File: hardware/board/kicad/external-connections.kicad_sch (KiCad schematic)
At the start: 34 parts, among them J1 KMDGX-6S-BS, J3 KMDGX-8S-BS, J4 TC2050-IDC-NL, J5 87520-0010BLF, U1 SN65HVD08DR, U2 LD1117S33TR_SOT223, U4 PTPSM863252RDXR

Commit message: Schematic cleanup
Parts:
- removed J4: TC2050-IDC-NL, Connector:Tag-Connect_TC2050-IDC-NL_2x05_P1.27mm_Vertical, symbol TC2050-IDC-NL:TC2050-IDC-NL
- C1, C14, C2, C7: value 100nF -> 100n
- C10: value 22pF -> 22p
- C11: value 33uF -> 33u
- C3, C8: value 10uF -> 10u
- C9: value 10nF -> 10n
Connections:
- net RS485_A: now also D1.2, J3.4, R18.1; no longer D1.1, R17.1, R5.2, U1.6 (A)
- net RS485_B: now also D1.1, J3.3, R17.1; no longer D1.2, R18.1, R5.1, U1.7 (B)
- net at R17.2: now also R5.1, U1.7 (B); no longer J3.4
- net at R18.2: now also R5.2, U1.6 (A); no longer J3.3
- no-connect marks 15 -> 12
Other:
- note added: "*DE Uses internal pull-up"
- note added: "12v to 5v Switching Regulator"
- note added: "5v to 3.3v LDO"
- note added: "External Pushbutton Connector"
- note added: "Input Pi Filter"
- note added: "RS485"
- note added: "RS485 and Power Connector"
- note added: "USB Charging Port"
- moved on the sheet: C10, C11, C12, C13, C14, C2, C3, C7, C8, C9, D1, D3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

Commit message: Finalized for review
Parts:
- L1: value 120 -> 120u
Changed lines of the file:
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@@
   (symbol (lib_id "Device:L_Ferrite") (at 247.015 39.751 90) (unit 1)
     (in_bom yes) (on_board yes) (dnp no) (fields_autoplaced)
-    (property "Reference" "L1" (at 247.015 33.401 90)
+    (property "Reference" "L1" (at 247.015 33.02 90)
       (effects (font (size 1.27 1.27)))
     )
-    (property "Value" "120" (at 247.015 35.941 90)
+    (property "Value" "120u" (at 247.015 35.56 90)
       (effects (font (size 1.27 1.27)))
     )

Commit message: Changed 2.2uF cap footprints and a bit more cleanup
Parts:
- C1, C14, C2, C7: Manufacturer_Name (none) -> AVX; Manufacturer_Part_Number (none) -> 08053C104KAT2A; Mouser Part Number (none) -> 581-08053C104K
- C10: Manufacturer_Name (none) -> Kemet; Manufacturer_Part_Number (none) -> C0603C220J4GACTU; Mouser Part Number (none) -> 80-C0603C220J4G
- C11: Manufacturer_Name (none) -> TDK; Manufacturer_Part_Number (none) -> C3216X5R1C336M160AB; Mouser Part Number (none) -> 810-C3216X5R1C336M
- C12, C13: footprint Capacitor_SMD:C_0603_1608Metric -> Capacitor_SMD:C_1206_3216Metric; Manufacturer_Name (none) -> Kemet; Manufacturer_Part_Number (none) -> C1206C225K3PACTU; Mouser Part Number (none) -> 80-C1206C225K3P
- C3, C8: Manufacturer_Name (none) -> Murata Electronics; Manufacturer_Part_Number (none) -> GRM319R61E106MA12D; Mouser Part Number (none) -> 81-GRM319R61E106MA2D
- C9: Manufacturer_Name (none) -> Kemet; Manufacturer_Part_Number (none) -> C0805C103J4GACTU; Mouser Part Number (none) -> 80-C0805C103J4G
- D3: Manufacturer_Name (none) -> Lite-On; Manufacturer_Part_Number (none) -> LTST-C150KRKT; Mouser Part Number (none) -> 859-LTST-C150KRKT
- F1: Manufacturer_Name (none) -> Littelfuse, Inc; Manufacturer_Part_Number (none) -> 1206L200SLYR; Mouser Part Number (none) -> 576-1206L200SLYR
- J1, J3: Manufacturer_Name Kycon -> Kycon, Inc.
- J5: Manufacturer_Name Amphenol Communications Solutions -> Amphenol ICC; Mouser Part Number (none) -> 649-87520-0010BLF
- L1: Manufacturer_Name (none) -> Bourns; Manufacturer_Part_Number (none) -> SRR1280A-121K; Mouser Part Number (none) -> 652-SRR1280A-121K
- R12, R4: Manufacturer_Name (none) -> Panasonic; Manufacturer_Part_Number (none) -> ERJ-PA3F1002V; Mouser Part Number (none) -> 667-ERJ-PA3F1002V
- R13: Manufacturer_Name (none) -> Panasonic; Manufacturer_Part_Number (none) -> ERJ-PA3F6192V; Mouser Part Number (none) -> 667-ERJ-PA3F6192V
- R14: Manufacturer_Name (none) -> Panasonic; Manufacturer_Part_Number (none) -> ERJ-PA3F2203V; Mouser Part Number (none) -> 667-ERJ-PA3F2203V
- R15: Manufacturer_Name (none) -> Panasonic; Manufacturer_Part_Number (none) -> ERJ-PA3F3002V; Mouser Part Number (none) -> 667-ERJ-PA3F3002V
- R16: value 157 -> 150; Manufacturer_Name (none) -> Panasonic; Manufacturer_Part_Number (none) -> ERJ-PA3F1500V; Mouser Part Number (none) -> 667-ERJ-PA3F1500V
- R17, R18: Manufacturer_Name (none) -> Panasonic; Manufacturer_Part_Number (none) -> ERJ-PA3F10R0V; Mouser Part Number (none) -> 667-ERJ-PA3F10R0V
- R19: Manufacturer_Name (none) -> Panasonic; Manufacturer_Part_Number (none) -> ERJ-P06F1500V; Mouser Part Number (none) -> 667-ERJ-P06F1500V
- R5: Manufacturer_Name (none) -> -; Manufacturer_Part_Number (none) -> -
- U2: Manufacturer_Name (none) -> STMicroelectronics; Manufacturer_Part_Number (none) -> LD1117S33TR; Mouser Part Number (none) -> 511-LD1117S33
- U4: Manufacturer_Name (none) -> Texas Instruments; Manufacturer_Part_Number (none) -> TPSM863252RDXR; Mouser Part Number (none) -> 595-TPSM863252RDXR

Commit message: Enabled pull-up resistor and removed lcd reset
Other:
- note added: "*DE and TX Use internal pull-ups"
- note removed: "*DE Uses internal pull-up"
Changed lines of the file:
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@@
     (effects (font (size 2.54 2.54)) (justify left bottom))
   )
-  (text "*DE Uses\ninternal pull-up" (at 54.483 44.45 0)
+  (text "*DE and TX Use\ninternal pull-ups" (at 54.483 46.482 0)
     (effects (font (size 1.27 1.27)) (justify right bottom))
   )

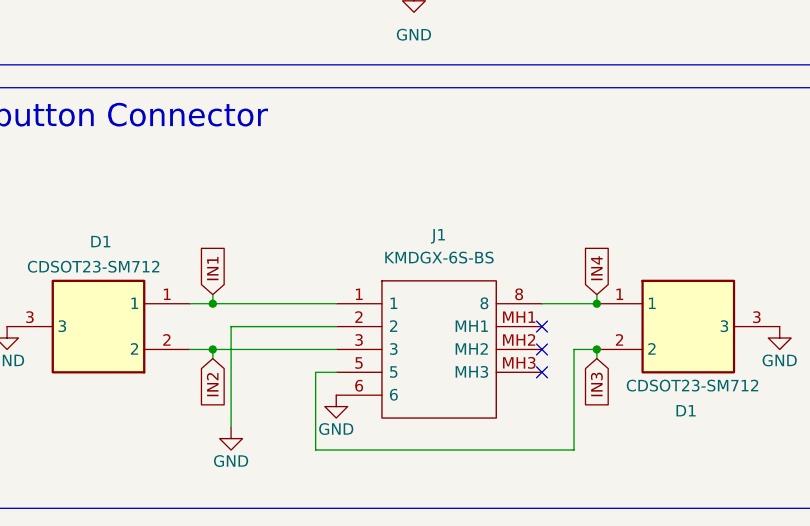
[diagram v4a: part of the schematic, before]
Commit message: Added inline resistors for ESD on inputs, created order T-V26W325984A
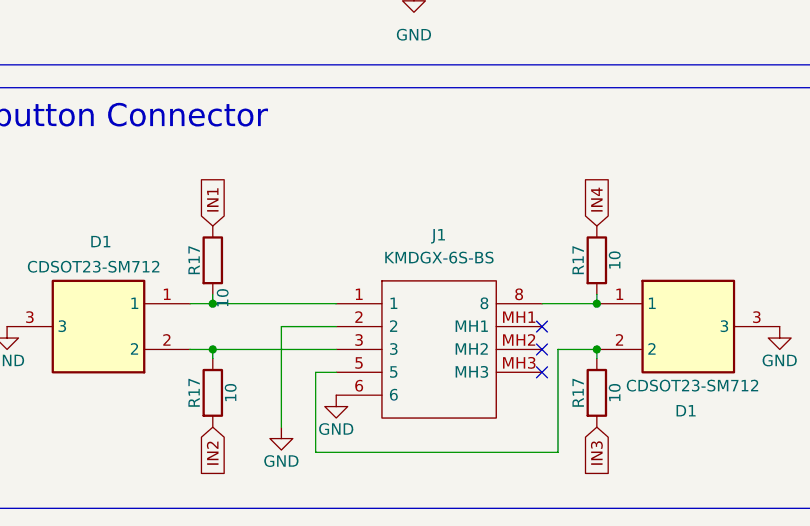
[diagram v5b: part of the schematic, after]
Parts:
- added R17 (x4): 10, Resistor_SMD:R_0603_1608Metric, symbol Device:R
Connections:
- net IN1: now also R17.1; no longer D1.1, J1.1
- net IN2: now also R17.2; no longer D1.2, J1.3
- net IN3: now also R17.2; no longer D1.2, J1.5
- net IN4: now also R17.1; no longer D1.1, J1.8
- new net: D1.2, J1.3, R17.1
- new net: D1.1, J1.1, R17.2
- new net: D1.1, J1.8, R17.2
- new net: D1.2, J1.5, R17.1

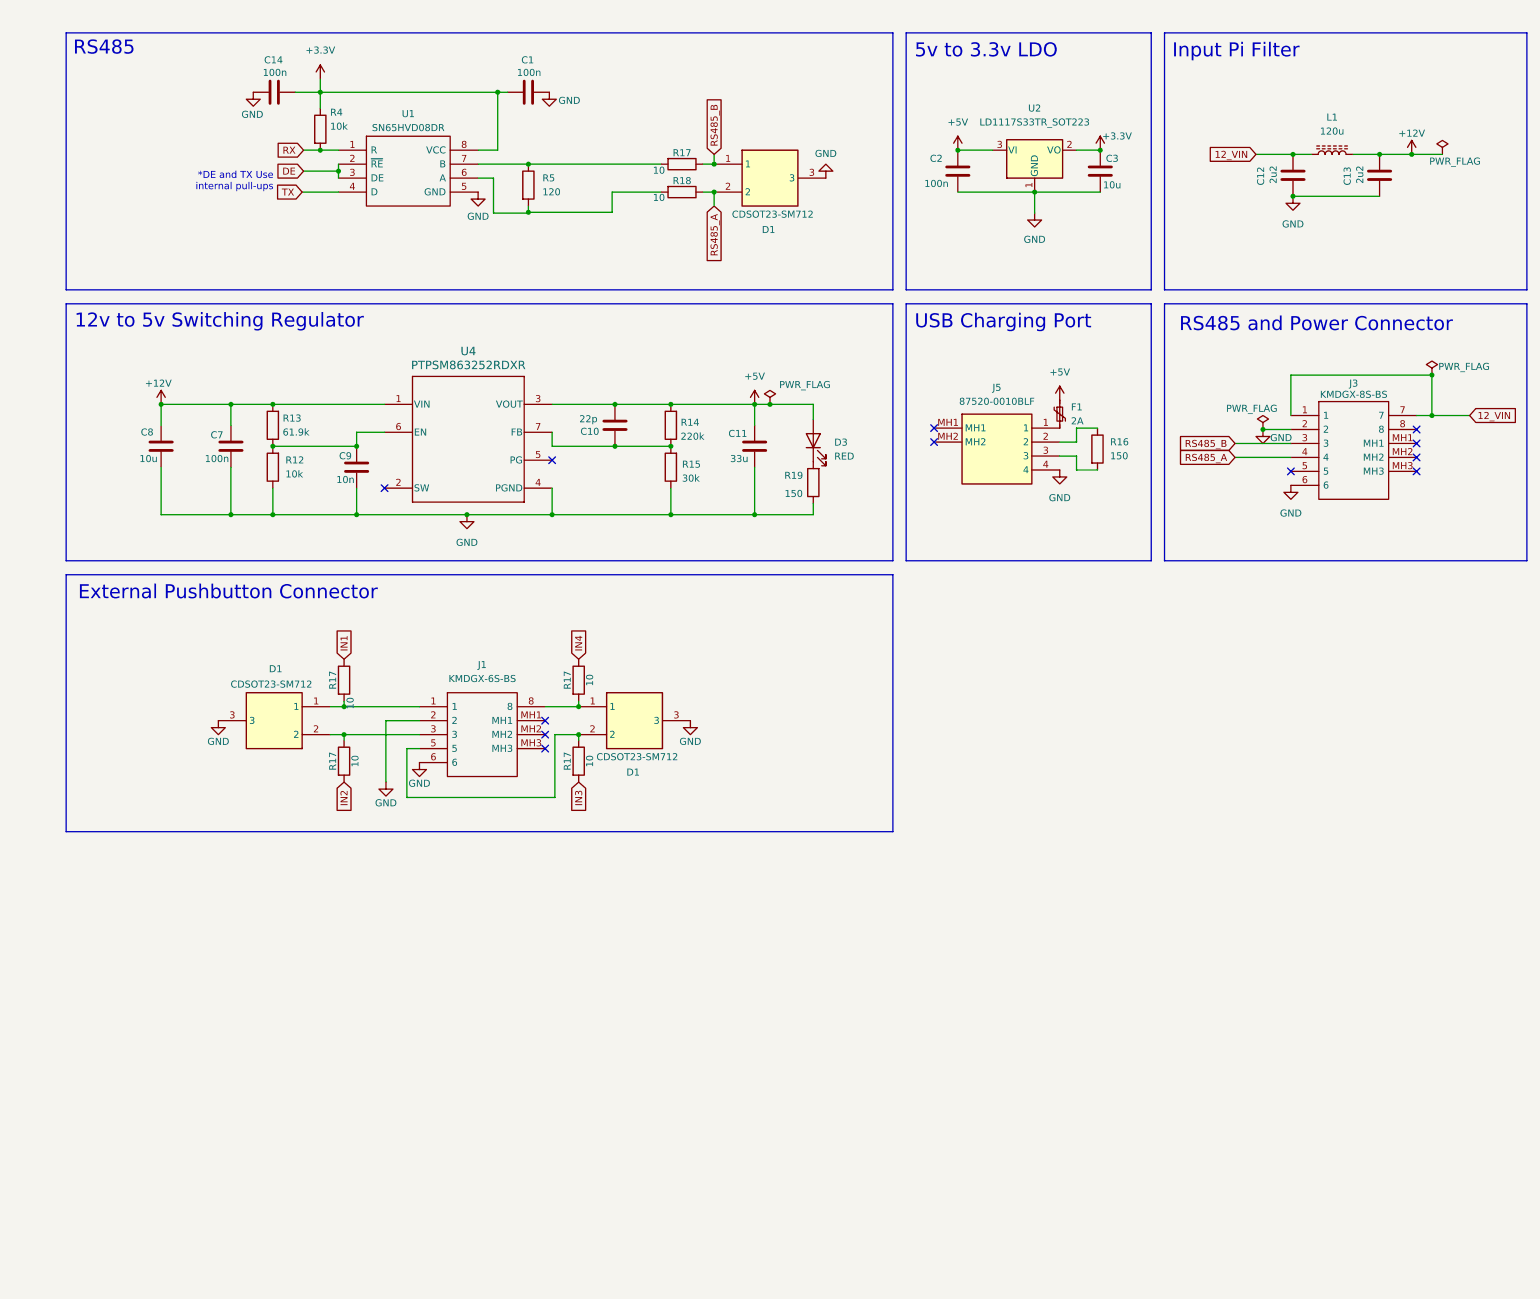
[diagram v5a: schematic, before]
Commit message: First pass at LM2596 regulator
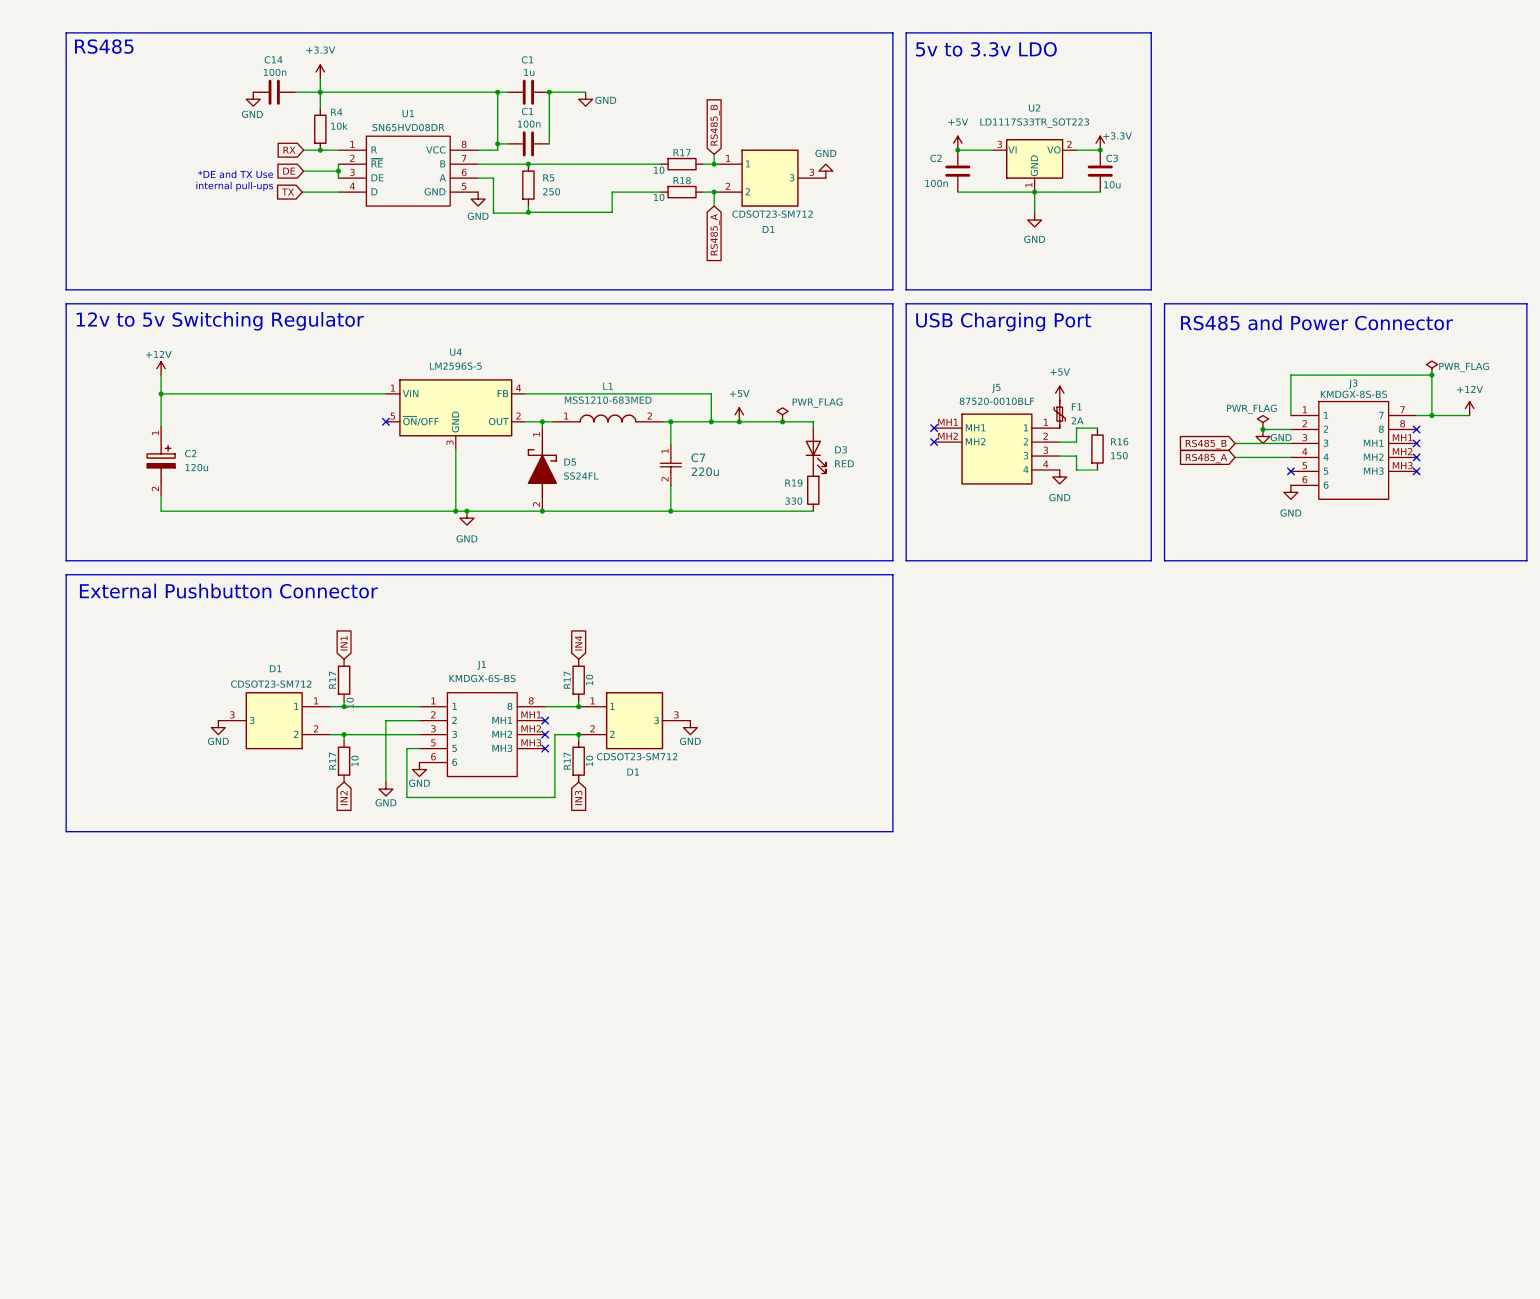
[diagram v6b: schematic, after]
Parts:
- removed C10: 22p, Capacitor_SMD:C_0603_1608Metric, symbol Device:C
- removed C11: 33u, Capacitor_SMD:C_1206_3216Metric, symbol Device:C
- removed C12, C13: 2u2, Capacitor_SMD:C_1206_3216Metric, symbol Device:C
- removed C7: 100n, Capacitor_SMD:C_0805_2012Metric, symbol Device:C
- removed C8: 10u, Capacitor_SMD:C_1206_3216Metric, symbol Device:C
- removed C9: 10n, Capacitor_SMD:C_0805_2012Metric, symbol Device:C
- removed L1: 120u, libs:L_Bourns_5050, symbol Device:L_Ferrite
- removed R12: 10k, Resistor_SMD:R_0603_1608Metric, symbol Device:R
- removed R13: 61.9k, Resistor_SMD:R_0603_1608Metric, symbol Device:R
- removed R14: 220k, Resistor_SMD:R_0603_1608Metric, symbol Device:R
- removed R15: 30k, Resistor_SMD:R_0603_1608Metric, symbol Device:R
- removed U4: PTPSM863252RDXR, libs:TPSM863252RDX, symbol TPSM863252RDX:PTPSM863252RDXR
- added C1: 100n, Capacitor_SMD:C_0805_2012Metric, symbol Device:C
- added C2: 120u, libs:16SVF180M, symbol 20SVPF120M:20SVPF120M
- added C7: 220u, libs:CHEMI-KE0, symbol 2024-02-06_04-13-04:EMVY630ARA221MKE0S
- added D5: SS24FL, libs:SODFL3617X108N, symbol SS24FL:SS24FL
- added L1: MSS1210-683MED, libs:INDPM120120X1020N, symbol MSS1210-683MED:MSS1210-683MED
- added U4: LM2596S-5, Package_TO_SOT_SMD:TO-263-5_TabPin3, symbol Regulator_Switching:LM2596S-5
- C1: value 100n -> 1u
- R19: value 150 -> 330
- R5: value 120 -> 250
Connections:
- net 12_VIN is gone; now on net +12V: J3.1, J3.7
- net +12V: now also C2.1 (+), U4.1 (VIN)
- net +3.3V: now also C1.2
- net +5V: now also C7.1, L1.2, U4.4 (FB)
- net GND: now also C1.1, C2.2 (-), C7.2, D5.2 (A), U4.3 (GND)
- new net: D5.1 (K), L1.1, U4.2 (OUT)
- no-connect marks 12 -> 11
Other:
- note removed: "Input Pi Filter"
- moved on the sheet: D3, R19
